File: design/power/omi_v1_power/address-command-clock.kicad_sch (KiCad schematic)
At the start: 2 parts

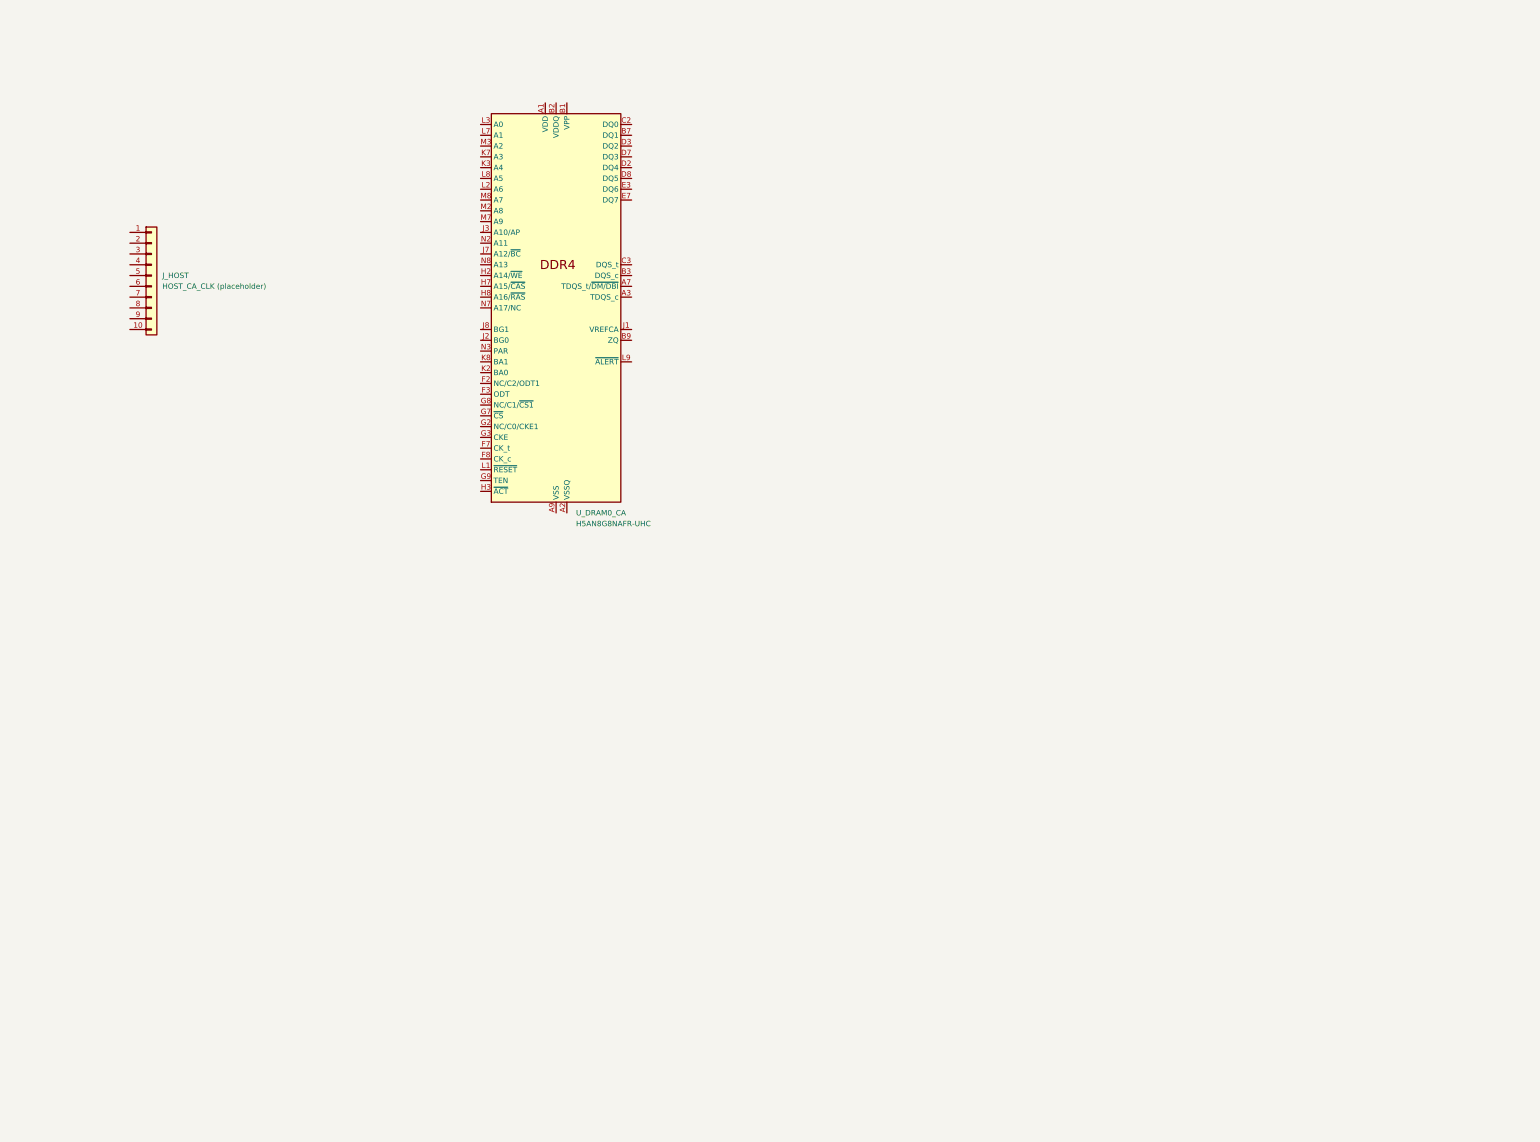
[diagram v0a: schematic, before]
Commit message: feat: Add OMI v1 Stage 7.2 CA/CLK checkpoint 01 documentation and PDF artifact.
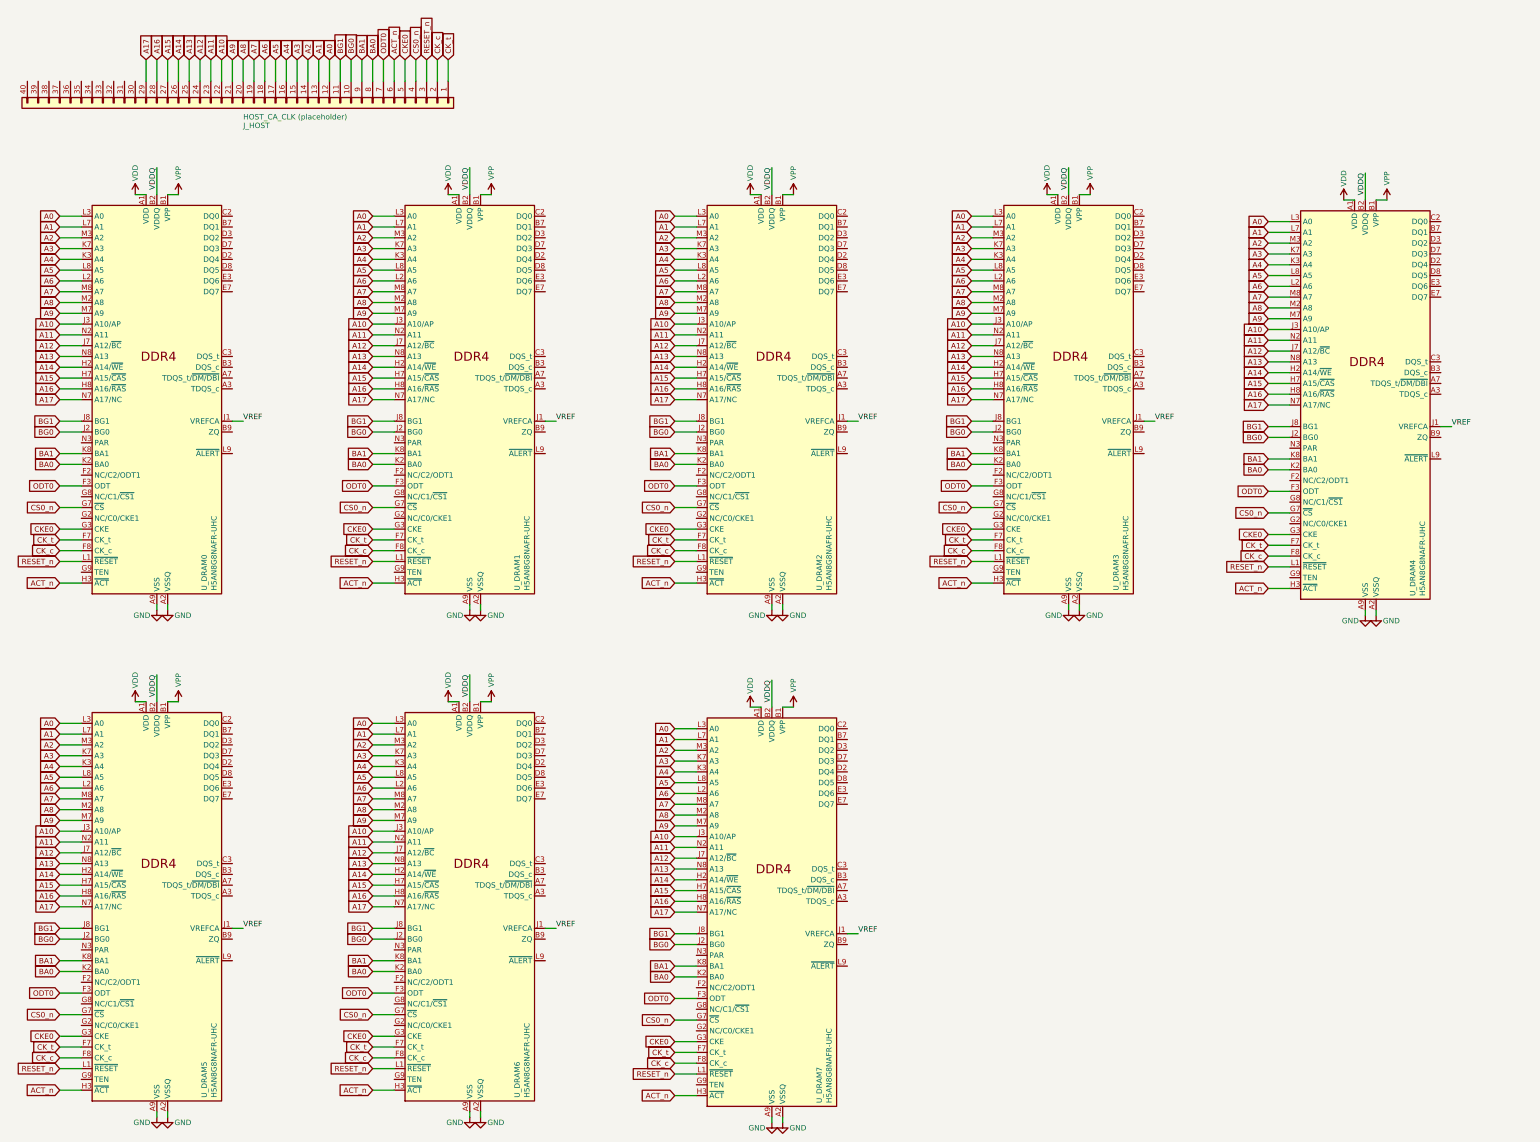
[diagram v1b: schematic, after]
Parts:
- removed J_HOST: HOST_CA_CLK (placeholder), symbol Connector_Generic:Conn_01x10
- removed U_DRAM0_CA: H5AN8G8NAFR-UHC, Package_BGA:FBGA-78_7.5x11mm_Layout2x3x13_P0.8mm, symbol Memory_RAM:H5AN8G8NAFR-UHC
- added J_HOST: HOST_CA_CLK (placeholder), symbol Connector_Generic:Conn_01x40
- added U_DRAM0, U_DRAM1, U_DRAM2, U_DRAM3, U_DRAM4, U_DRAM5, U_DRAM6, U_DRAM7: H5AN8G8NAFR-UHC, Package_BGA:FBGA-78_7.5x11mm_Layout2x3x13_P0.8mm, symbol Memory_RAM:H5AN8G8NAFR-UHC
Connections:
- new net A0: J_HOST.12 (Pin_12), U_DRAM0.L3 (A0), U_DRAM1.L3 (A0), U_DRAM2.L3 (A0), U_DRAM3.L3 (A0), U_DRAM4.L3 (A0), U_DRAM5.L3 (A0), U_DRAM6.L3 (A0), U_DRAM7.L3 (A0)
- new net A1: J_HOST.13 (Pin_13), U_DRAM0.L7 (A1), U_DRAM1.L7 (A1), U_DRAM2.L7 (A1), U_DRAM3.L7 (A1), U_DRAM4.L7 (A1), U_DRAM5.L7 (A1), U_DRAM6.L7 (A1), U_DRAM7.L7 (A1)
- new net A10: J_HOST.22 (Pin_22), U_DRAM0.J3 (A10/AP), U_DRAM1.J3 (A10/AP), U_DRAM2.J3 (A10/AP), U_DRAM3.J3 (A10/AP), U_DRAM4.J3 (A10/AP), U_DRAM5.J3 (A10/AP), U_DRAM6.J3 (A10/AP), U_DRAM7.J3 (A10/AP)
- new net A11: J_HOST.23 (Pin_23), U_DRAM0.N2 (A11), U_DRAM1.N2 (A11), U_DRAM2.N2 (A11), U_DRAM3.N2 (A11), U_DRAM4.N2 (A11), U_DRAM5.N2 (A11), U_DRAM6.N2 (A11), U_DRAM7.N2 (A11)
- new net A12: J_HOST.24 (Pin_24), U_DRAM0.J7 (A12/~{BC}), U_DRAM1.J7 (A12/~{BC}), U_DRAM2.J7 (A12/~{BC}), U_DRAM3.J7 (A12/~{BC}), U_DRAM4.J7 (A12/~{BC}), U_DRAM5.J7 (A12/~{BC}), U_DRAM6.J7 (A12/~{BC}), U_DRAM7.J7 (A12/~{BC})
- new net A13: J_HOST.25 (Pin_25), U_DRAM0.N8 (A13), U_DRAM1.N8 (A13), U_DRAM2.N8 (A13), U_DRAM3.N8 (A13), U_DRAM4.N8 (A13), U_DRAM5.N8 (A13), U_DRAM6.N8 (A13), U_DRAM7.N8 (A13)
- new net A14: J_HOST.26 (Pin_26), U_DRAM0.H2 (A14/~{WE}), U_DRAM1.H2 (A14/~{WE}), U_DRAM2.H2 (A14/~{WE}), U_DRAM3.H2 (A14/~{WE}), U_DRAM4.H2 (A14/~{WE}), U_DRAM5.H2 (A14/~{WE}), U_DRAM6.H2 (A14/~{WE}), U_DRAM7.H2 (A14/~{WE})
- new net A15: J_HOST.27 (Pin_27), U_DRAM0.H7 (A15/~{CAS}), U_DRAM1.H7 (A15/~{CAS}), U_DRAM2.H7 (A15/~{CAS}), U_DRAM3.H7 (A15/~{CAS}), U_DRAM4.H7 (A15/~{CAS}), U_DRAM5.H7 (A15/~{CAS}), U_DRAM6.H7 (A15/~{CAS}), U_DRAM7.H7 (A15/~{CAS})
- new net A16: J_HOST.28 (Pin_28), U_DRAM0.H8 (A16/~{RAS}), U_DRAM1.H8 (A16/~{RAS}), U_DRAM2.H8 (A16/~{RAS}), U_DRAM3.H8 (A16/~{RAS}), U_DRAM4.H8 (A16/~{RAS}), U_DRAM5.H8 (A16/~{RAS}), U_DRAM6.H8 (A16/~{RAS}), U_DRAM7.H8 (A16/~{RAS})
- new net A17: J_HOST.29 (Pin_29), U_DRAM0.N7 (A17/NC), U_DRAM1.N7 (A17/NC), U_DRAM2.N7 (A17/NC), U_DRAM3.N7 (A17/NC), U_DRAM4.N7 (A17/NC), U_DRAM5.N7 (A17/NC), U_DRAM6.N7 (A17/NC), U_DRAM7.N7 (A17/NC)
- new net A2: J_HOST.14 (Pin_14), U_DRAM0.M3 (A2), U_DRAM1.M3 (A2), U_DRAM2.M3 (A2), U_DRAM3.M3 (A2), U_DRAM4.M3 (A2), U_DRAM5.M3 (A2), U_DRAM6.M3 (A2), U_DRAM7.M3 (A2)
- new net A3: J_HOST.15 (Pin_15), U_DRAM0.K7 (A3), U_DRAM1.K7 (A3), U_DRAM2.K7 (A3), U_DRAM3.K7 (A3), U_DRAM4.K7 (A3), U_DRAM5.K7 (A3), U_DRAM6.K7 (A3), U_DRAM7.K7 (A3)
- new net A4: J_HOST.16 (Pin_16), U_DRAM0.K3 (A4), U_DRAM1.K3 (A4), U_DRAM2.K3 (A4), U_DRAM3.K3 (A4), U_DRAM4.K3 (A4), U_DRAM5.K3 (A4), U_DRAM6.K3 (A4), U_DRAM7.K3 (A4)
- new net A5: J_HOST.17 (Pin_17), U_DRAM0.L8 (A5), U_DRAM1.L8 (A5), U_DRAM2.L8 (A5), U_DRAM3.L8 (A5), U_DRAM4.L8 (A5), U_DRAM5.L8 (A5), U_DRAM6.L8 (A5), U_DRAM7.L8 (A5)
- new net A6: J_HOST.18 (Pin_18), U_DRAM0.L2 (A6), U_DRAM1.L2 (A6), U_DRAM2.L2 (A6), U_DRAM3.L2 (A6), U_DRAM4.L2 (A6), U_DRAM5.L2 (A6), U_DRAM6.L2 (A6), U_DRAM7.L2 (A6)
- new net A7: J_HOST.19 (Pin_19), U_DRAM0.M8 (A7), U_DRAM1.M8 (A7), U_DRAM2.M8 (A7), U_DRAM3.M8 (A7), U_DRAM4.M8 (A7), U_DRAM5.M8 (A7), U_DRAM6.M8 (A7), U_DRAM7.M8 (A7)
- new net A8: J_HOST.20 (Pin_20), U_DRAM0.M2 (A8), U_DRAM1.M2 (A8), U_DRAM2.M2 (A8), U_DRAM3.M2 (A8), U_DRAM4.M2 (A8), U_DRAM5.M2 (A8), U_DRAM6.M2 (A8), U_DRAM7.M2 (A8)
- new net A9: J_HOST.21 (Pin_21), U_DRAM0.M7 (A9), U_DRAM1.M7 (A9), U_DRAM2.M7 (A9), U_DRAM3.M7 (A9), U_DRAM4.M7 (A9), U_DRAM5.M7 (A9), U_DRAM6.M7 (A9), U_DRAM7.M7 (A9)
- new net ACT_n: J_HOST.6 (Pin_6), U_DRAM0.H3 (~{ACT}), U_DRAM1.H3 (~{ACT}), U_DRAM2.H3 (~{ACT}), U_DRAM3.H3 (~{ACT}), U_DRAM4.H3 (~{ACT}), U_DRAM5.H3 (~{ACT}), U_DRAM6.H3 (~{ACT}), U_DRAM7.H3 (~{ACT})
- new net BA0: J_HOST.8 (Pin_8), U_DRAM0.K2 (BA0), U_DRAM1.K2 (BA0), U_DRAM2.K2 (BA0), U_DRAM3.K2 (BA0), U_DRAM4.K2 (BA0), U_DRAM5.K2 (BA0), U_DRAM6.K2 (BA0), U_DRAM7.K2 (BA0)
- new net BA1: J_HOST.9 (Pin_9), U_DRAM0.K8 (BA1), U_DRAM1.K8 (BA1), U_DRAM2.K8 (BA1), U_DRAM3.K8 (BA1), U_DRAM4.K8 (BA1), U_DRAM5.K8 (BA1), U_DRAM6.K8 (BA1), U_DRAM7.K8 (BA1)
- new net BG0: J_HOST.10 (Pin_10), U_DRAM0.J2 (BG0), U_DRAM1.J2 (BG0), U_DRAM2.J2 (BG0), U_DRAM3.J2 (BG0), U_DRAM4.J2 (BG0), U_DRAM5.J2 (BG0), U_DRAM6.J2 (BG0), U_DRAM7.J2 (BG0)
- new net BG1: J_HOST.11 (Pin_11), U_DRAM0.J8 (BG1), U_DRAM1.J8 (BG1), U_DRAM2.J8 (BG1), U_DRAM3.J8 (BG1), U_DRAM4.J8 (BG1), U_DRAM5.J8 (BG1), U_DRAM6.J8 (BG1), U_DRAM7.J8 (BG1)
- new net CKE0: J_HOST.5 (Pin_5), U_DRAM0.G3 (CKE), U_DRAM1.G3 (CKE), U_DRAM2.G3 (CKE), U_DRAM3.G3 (CKE), U_DRAM4.G3 (CKE), U_DRAM5.G3 (CKE), U_DRAM6.G3 (CKE), U_DRAM7.G3 (CKE)
- new net CK_c: J_HOST.2 (Pin_2), U_DRAM0.F8 (CK_c), U_DRAM1.F8 (CK_c), U_DRAM2.F8 (CK_c), U_DRAM3.F8 (CK_c), U_DRAM4.F8 (CK_c), U_DRAM5.F8 (CK_c), U_DRAM6.F8 (CK_c), U_DRAM7.F8 (CK_c)
- new net CK_t: J_HOST.1 (Pin_1), U_DRAM0.F7 (CK_t), U_DRAM1.F7 (CK_t), U_DRAM2.F7 (CK_t), U_DRAM3.F7 (CK_t), U_DRAM4.F7 (CK_t), U_DRAM5.F7 (CK_t), U_DRAM6.F7 (CK_t), U_DRAM7.F7 (CK_t)
- new net CS0_n: J_HOST.4 (Pin_4), U_DRAM0.G7 (~{CS}), U_DRAM1.G7 (~{CS}), U_DRAM2.G7 (~{CS}), U_DRAM3.G7 (~{CS}), U_DRAM4.G7 (~{CS}), U_DRAM5.G7 (~{CS}), U_DRAM6.G7 (~{CS}), U_DRAM7.G7 (~{CS})
- new net GND: U_DRAM0.A2 (VSSQ), U_DRAM0.A8 (VSSQ), U_DRAM0.A9 (VSS), U_DRAM0.C8 (VSS), U_DRAM0.D1 (VSSQ), U_DRAM0.D9 (VSSQ), U_DRAM0.E1 (VSS), U_DRAM0.E9 (VSS), U_DRAM0.G1 (VSS), U_DRAM0.H9 (VSS), U_DRAM0.K1 (VSS), U_DRAM0.K9 (VSS), U_DRAM0.N1 (VSS), U_DRAM1.A2 (VSSQ), U_DRAM1.A8 (VSSQ), U_DRAM1.A9 (VSS), U_DRAM1.C8 (VSS), U_DRAM1.D1 (VSSQ), U_DRAM1.D9 (VSSQ), U_DRAM1.E1 (VSS), U_DRAM1.E9 (VSS), U_DRAM1.G1 (VSS), U_DRAM1.H9 (VSS), U_DRAM1.K1 (VSS), U_DRAM1.K9 (VSS), U_DRAM1.N1 (VSS), U_DRAM2.A2 (VSSQ), U_DRAM2.A8 (VSSQ), U_DRAM2.A9 (VSS), U_DRAM2.C8 (VSS), U_DRAM2.D1 (VSSQ), U_DRAM2.D9 (VSSQ), U_DRAM2.E1 (VSS), U_DRAM2.E9 (VSS), U_DRAM2.G1 (VSS), U_DRAM2.H9 (VSS), U_DRAM2.K1 (VSS), U_DRAM2.K9 (VSS), U_DRAM2.N1 (VSS), U_DRAM3.A2 (VSSQ), U_DRAM3.A8 (VSSQ), U_DRAM3.A9 (VSS), U_DRAM3.C8 (VSS), U_DRAM3.D1 (VSSQ), U_DRAM3.D9 (VSSQ), U_DRAM3.E1 (VSS), U_DRAM3.E9 (VSS), U_DRAM3.G1 (VSS), U_DRAM3.H9 (VSS), U_DRAM3.K1 (VSS), U_DRAM3.K9 (VSS), U_DRAM3.N1 (VSS), U_DRAM4.A2 (VSSQ), U_DRAM4.A8 (VSSQ), U_DRAM4.A9 (VSS), U_DRAM4.C8 (VSS), U_DRAM4.D1 (VSSQ), U_DRAM4.D9 (VSSQ), U_DRAM4.E1 (VSS), U_DRAM4.E9 (VSS), U_DRAM4.G1 (VSS), U_DRAM4.H9 (VSS), U_DRAM4.K1 (VSS), U_DRAM4.K9 (VSS), U_DRAM4.N1 (VSS), U_DRAM5.A2 (VSSQ), U_DRAM5.A8 (VSSQ), U_DRAM5.A9 (VSS), U_DRAM5.C8 (VSS), U_DRAM5.D1 (VSSQ), U_DRAM5.D9 (VSSQ), U_DRAM5.E1 (VSS), U_DRAM5.E9 (VSS), U_DRAM5.G1 (VSS), U_DRAM5.H9 (VSS), U_DRAM5.K1 (VSS), U_DRAM5.K9 (VSS), U_DRAM5.N1 (VSS), U_DRAM6.A2 (VSSQ), U_DRAM6.A8 (VSSQ), U_DRAM6.A9 (VSS), U_DRAM6.C8 (VSS), U_DRAM6.D1 (VSSQ), U_DRAM6.D9 (VSSQ), U_DRAM6.E1 (VSS), U_DRAM6.E9 (VSS), U_DRAM6.G1 (VSS), U_DRAM6.H9 (VSS), U_DRAM6.K1 (VSS), U_DRAM6.K9 (VSS), U_DRAM6.N1 (VSS), U_DRAM7.A2 (VSSQ), U_DRAM7.A8 (VSSQ), U_DRAM7.A9 (VSS), U_DRAM7.C8 (VSS), U_DRAM7.D1 (VSSQ), U_DRAM7.D9 (VSSQ), U_DRAM7.E1 (VSS), U_DRAM7.E9 (VSS), U_DRAM7.G1 (VSS), U_DRAM7.H9 (VSS), U_DRAM7.K1 (VSS), U_DRAM7.K9 (VSS), U_DRAM7.N1 (VSS)
- new net ODT0: J_HOST.7 (Pin_7), U_DRAM0.F3 (ODT), U_DRAM1.F3 (ODT), U_DRAM2.F3 (ODT), U_DRAM3.F3 (ODT), U_DRAM4.F3 (ODT), U_DRAM5.F3 (ODT), U_DRAM6.F3 (ODT), U_DRAM7.F3 (ODT)
- new net RESET_n: J_HOST.3 (Pin_3), U_DRAM0.L1 (~{RESET}), U_DRAM1.L1 (~{RESET}), U_DRAM2.L1 (~{RESET}), U_DRAM3.L1 (~{RESET}), U_DRAM4.L1 (~{RESET}), U_DRAM5.L1 (~{RESET}), U_DRAM6.L1 (~{RESET}), U_DRAM7.L1 (~{RESET})
- new net VDD: U_DRAM0.A1 (VDD), U_DRAM0.C7 (VDD), U_DRAM0.F1 (VDD), U_DRAM0.F9 (VDD), U_DRAM0.H1 (VDD), U_DRAM0.J9 (VDD), U_DRAM0.M1 (VDD), U_DRAM0.N9 (VDD), U_DRAM1.A1 (VDD), U_DRAM1.C7 (VDD), U_DRAM1.F1 (VDD), U_DRAM1.F9 (VDD), U_DRAM1.H1 (VDD), U_DRAM1.J9 (VDD), U_DRAM1.M1 (VDD), U_DRAM1.N9 (VDD), U_DRAM2.A1 (VDD), U_DRAM2.C7 (VDD), U_DRAM2.F1 (VDD), U_DRAM2.F9 (VDD), U_DRAM2.H1 (VDD), U_DRAM2.J9 (VDD), U_DRAM2.M1 (VDD), U_DRAM2.N9 (VDD), U_DRAM3.A1 (VDD), U_DRAM3.C7 (VDD), U_DRAM3.F1 (VDD), U_DRAM3.F9 (VDD), U_DRAM3.H1 (VDD), U_DRAM3.J9 (VDD), U_DRAM3.M1 (VDD), U_DRAM3.N9 (VDD), U_DRAM4.A1 (VDD), U_DRAM4.C7 (VDD), U_DRAM4.F1 (VDD), U_DRAM4.F9 (VDD), U_DRAM4.H1 (VDD), U_DRAM4.J9 (VDD), U_DRAM4.M1 (VDD), U_DRAM4.N9 (VDD), U_DRAM5.A1 (VDD), U_DRAM5.C7 (VDD), U_DRAM5.F1 (VDD), U_DRAM5.F9 (VDD), U_DRAM5.H1 (VDD), U_DRAM5.J9 (VDD), U_DRAM5.M1 (VDD), U_DRAM5.N9 (VDD), U_DRAM6.A1 (VDD), U_DRAM6.C7 (VDD), U_DRAM6.F1 (VDD), U_DRAM6.F9 (VDD), U_DRAM6.H1 (VDD), U_DRAM6.J9 (VDD), U_DRAM6.M1 (VDD), U_DRAM6.N9 (VDD), U_DRAM7.A1 (VDD), U_DRAM7.C7 (VDD), U_DRAM7.F1 (VDD), U_DRAM7.F9 (VDD), U_DRAM7.H1 (VDD), U_DRAM7.J9 (VDD), U_DRAM7.M1 (VDD), U_DRAM7.N9 (VDD)
- new net VDDQ: U_DRAM0.B2 (VDDQ), U_DRAM0.B8 (VDDQ), U_DRAM0.C1 (VDDQ), U_DRAM0.C9 (VDDQ), U_DRAM0.E2 (VDDQ), U_DRAM0.E8 (VDDQ), U_DRAM1.B2 (VDDQ), U_DRAM1.B8 (VDDQ), U_DRAM1.C1 (VDDQ), U_DRAM1.C9 (VDDQ), U_DRAM1.E2 (VDDQ), U_DRAM1.E8 (VDDQ), U_DRAM2.B2 (VDDQ), U_DRAM2.B8 (VDDQ), U_DRAM2.C1 (VDDQ), U_DRAM2.C9 (VDDQ), U_DRAM2.E2 (VDDQ), U_DRAM2.E8 (VDDQ), U_DRAM3.B2 (VDDQ), U_DRAM3.B8 (VDDQ), U_DRAM3.C1 (VDDQ), U_DRAM3.C9 (VDDQ), U_DRAM3.E2 (VDDQ), U_DRAM3.E8 (VDDQ), U_DRAM4.B2 (VDDQ), U_DRAM4.B8 (VDDQ), U_DRAM4.C1 (VDDQ), U_DRAM4.C9 (VDDQ), U_DRAM4.E2 (VDDQ), U_DRAM4.E8 (VDDQ), U_DRAM5.B2 (VDDQ), U_DRAM5.B8 (VDDQ), U_DRAM5.C1 (VDDQ), U_DRAM5.C9 (VDDQ), U_DRAM5.E2 (VDDQ), U_DRAM5.E8 (VDDQ), U_DRAM6.B2 (VDDQ), U_DRAM6.B8 (VDDQ), U_DRAM6.C1 (VDDQ), U_DRAM6.C9 (VDDQ), U_DRAM6.E2 (VDDQ), U_DRAM6.E8 (VDDQ), U_DRAM7.B2 (VDDQ), U_DRAM7.B8 (VDDQ), U_DRAM7.C1 (VDDQ), U_DRAM7.C9 (VDDQ), U_DRAM7.E2 (VDDQ), U_DRAM7.E8 (VDDQ)
- new net VPP: U_DRAM0.B1 (VPP), U_DRAM0.M9 (VPP), U_DRAM1.B1 (VPP), U_DRAM1.M9 (VPP), U_DRAM2.B1 (VPP), U_DRAM2.M9 (VPP), U_DRAM3.B1 (VPP), U_DRAM3.M9 (VPP), U_DRAM4.B1 (VPP), U_DRAM4.M9 (VPP), U_DRAM5.B1 (VPP), U_DRAM5.M9 (VPP), U_DRAM6.B1 (VPP), U_DRAM6.M9 (VPP), U_DRAM7.B1 (VPP), U_DRAM7.M9 (VPP)
- new net VREF: U_DRAM0.J1 (VREFCA), U_DRAM1.J1 (VREFCA), U_DRAM2.J1 (VREFCA), U_DRAM3.J1 (VREFCA), U_DRAM4.J1 (VREFCA), U_DRAM5.J1 (VREFCA), U_DRAM6.J1 (VREFCA), U_DRAM7.J1 (VREFCA)

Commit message: feat: Add OMI v1 Stage 7.3 DQ/DQS documentation and PDF artifact.
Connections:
- net D7_DM_DBI_n: now reaches U_DRAM7.A7 (TDQS_t/~{DM/DBI})
- net D7_DQS_c: now reaches U_DRAM7.B3 (DQS_c)
- net D7_DQ1: now reaches U_DRAM7.B7 (DQ1)
- net D7_DQ0: now reaches U_DRAM7.C2 (DQ0)
- net D7_DQS_t: now reaches U_DRAM7.C3 (DQS_t)
- net D7_DQ4: now reaches U_DRAM7.D2 (DQ4)
- net D7_DQ2: now reaches U_DRAM7.D3 (DQ2)
- net D7_DQ3: now reaches U_DRAM7.D7 (DQ3)
- net D7_DQ5: now reaches U_DRAM7.D8 (DQ5)
- net D7_DQ6: now reaches U_DRAM7.E3 (DQ6)
- net D7_DQ7: now reaches U_DRAM7.E7 (DQ7)
- net D3_DM_DBI_n: now reaches U_DRAM3.A7 (TDQS_t/~{DM/DBI})
- net D3_DQS_c: now reaches U_DRAM3.B3 (DQS_c)
- net D3_DQ1: now reaches U_DRAM3.B7 (DQ1)
- net D3_DQ0: now reaches U_DRAM3.C2 (DQ0)
- net D3_DQS_t: now reaches U_DRAM3.C3 (DQS_t)
- net D3_DQ4: now reaches U_DRAM3.D2 (DQ4)
- net D3_DQ2: now reaches U_DRAM3.D3 (DQ2)
- net D3_DQ3: now reaches U_DRAM3.D7 (DQ3)
- net D3_DQ5: now reaches U_DRAM3.D8 (DQ5)
- net D3_DQ6: now reaches U_DRAM3.E3 (DQ6)
- net D3_DQ7: now reaches U_DRAM3.E7 (DQ7)
- net D2_DM_DBI_n: now reaches U_DRAM2.A7 (TDQS_t/~{DM/DBI})
- net D2_DQS_c: now reaches U_DRAM2.B3 (DQS_c)
- net D2_DQ1: now reaches U_DRAM2.B7 (DQ1)
- net D2_DQ0: now reaches U_DRAM2.C2 (DQ0)
- net D2_DQS_t: now reaches U_DRAM2.C3 (DQS_t)
- net D2_DQ4: now reaches U_DRAM2.D2 (DQ4)
- net D2_DQ2: now reaches U_DRAM2.D3 (DQ2)
- net D2_DQ3: now reaches U_DRAM2.D7 (DQ3)
- net D2_DQ5: now reaches U_DRAM2.D8 (DQ5)
- net D2_DQ6: now reaches U_DRAM2.E3 (DQ6)
- net D2_DQ7: now reaches U_DRAM2.E7 (DQ7)
- net D4_DM_DBI_n: now reaches U_DRAM4.A7 (TDQS_t/~{DM/DBI})
- net D4_DQS_c: now reaches U_DRAM4.B3 (DQS_c)
- net D4_DQ1: now reaches U_DRAM4.B7 (DQ1)
- net D4_DQ0: now reaches U_DRAM4.C2 (DQ0)
- net D4_DQS_t: now reaches U_DRAM4.C3 (DQS_t)
- net D4_DQ4: now reaches U_DRAM4.D2 (DQ4)
- net D4_DQ2: now reaches U_DRAM4.D3 (DQ2)
- net D4_DQ3: now reaches U_DRAM4.D7 (DQ3)
- net D4_DQ5: now reaches U_DRAM4.D8 (DQ5)
- net D4_DQ6: now reaches U_DRAM4.E3 (DQ6)
- net D4_DQ7: now reaches U_DRAM4.E7 (DQ7)
- net D5_DM_DBI_n: now reaches U_DRAM5.A7 (TDQS_t/~{DM/DBI})
- net D5_DQS_c: now reaches U_DRAM5.B3 (DQS_c)
- net D5_DQ1: now reaches U_DRAM5.B7 (DQ1)
- net D5_DQ0: now reaches U_DRAM5.C2 (DQ0)
- net D5_DQS_t: now reaches U_DRAM5.C3 (DQS_t)
- net D5_DQ4: now reaches U_DRAM5.D2 (DQ4)
- net D5_DQ2: now reaches U_DRAM5.D3 (DQ2)
- net D5_DQ3: now reaches U_DRAM5.D7 (DQ3)
- net D5_DQ5: now reaches U_DRAM5.D8 (DQ5)
- net D5_DQ6: now reaches U_DRAM5.E3 (DQ6)
- net D5_DQ7: now reaches U_DRAM5.E7 (DQ7)
- net D1_DM_DBI_n: now reaches U_DRAM1.A7 (TDQS_t/~{DM/DBI})
- net D1_DQS_c: now reaches U_DRAM1.B3 (DQS_c)
- net D1_DQ1: now reaches U_DRAM1.B7 (DQ1)
- net D1_DQ0: now reaches U_DRAM1.C2 (DQ0)
- net D1_DQS_t: now reaches U_DRAM1.C3 (DQS_t)
- net D1_DQ4: now reaches U_DRAM1.D2 (DQ4)
- net D1_DQ2: now reaches U_DRAM1.D3 (DQ2)
- net D1_DQ3: now reaches U_DRAM1.D7 (DQ3)
- net D1_DQ5: now reaches U_DRAM1.D8 (DQ5)
- net D1_DQ6: now reaches U_DRAM1.E3 (DQ6)
- net D1_DQ7: now reaches U_DRAM1.E7 (DQ7)
- net D0_DM_DBI_n: now reaches U_DRAM0.A7 (TDQS_t/~{DM/DBI})
- net D0_DQS_c: now reaches U_DRAM0.B3 (DQS_c)
- net D0_DQ1: now reaches U_DRAM0.B7 (DQ1)
- net D0_DQ0: now reaches U_DRAM0.C2 (DQ0)
- net D0_DQS_t: now reaches U_DRAM0.C3 (DQS_t)
- net D0_DQ4: now reaches U_DRAM0.D2 (DQ4)
- net D0_DQ2: now reaches U_DRAM0.D3 (DQ2)
- net D0_DQ3: now reaches U_DRAM0.D7 (DQ3)
- net D0_DQ5: now reaches U_DRAM0.D8 (DQ5)
- net D0_DQ6: now reaches U_DRAM0.E3 (DQ6)
- net D0_DQ7: now reaches U_DRAM0.E7 (DQ7)
- net D6_DM_DBI_n: now reaches U_DRAM6.A7 (TDQS_t/~{DM/DBI})
- net D6_DQS_c: now reaches U_DRAM6.B3 (DQS_c)
- net D6_DQ1: now reaches U_DRAM6.B7 (DQ1)
- net D6_DQ0: now reaches U_DRAM6.C2 (DQ0)
- net D6_DQS_t: now reaches U_DRAM6.C3 (DQS_t)
- net D6_DQ4: now reaches U_DRAM6.D2 (DQ4)
- net D6_DQ2: now reaches U_DRAM6.D3 (DQ2)
- net D6_DQ3: now reaches U_DRAM6.D7 (DQ3)
- net D6_DQ5: now reaches U_DRAM6.D8 (DQ5)
- net D6_DQ6: now reaches U_DRAM6.E3 (DQ6)
- net D6_DQ7: now reaches U_DRAM6.E7 (DQ7)
